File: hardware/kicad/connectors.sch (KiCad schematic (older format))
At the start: 1 part, among them J1 Conn_01x13_Male

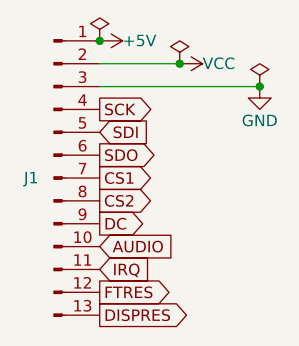
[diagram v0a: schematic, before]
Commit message: Clean up board and expose less debug signals
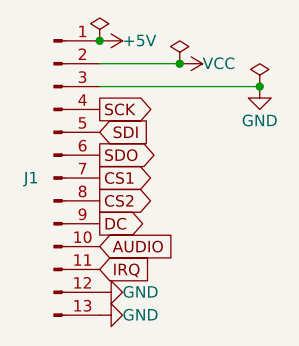
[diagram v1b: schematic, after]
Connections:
- net DISPRES is gone; now on net GND: J1.13 (Pin_13)
- net FTRES is gone; now on net GND: J1.12 (Pin_12)
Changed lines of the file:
@@
 Text GLabel 5650 4400 2    50   Input ~ 0
 IRQ
-Text GLabel 5650 4500 2    50   Output ~ 0
-FTRES
-Text GLabel 5650 4600 2    50   Output ~ 0
-DISPRES
+$Comp
+L power:GND #PWR029
+U 1 1 5F146BD0
+P 5650 4500
+F 0 "#PWR029" H 5650 4250 50  0001 C CNN
+F 1 "GND" V 5650 4400 50  0000 R CNN
+F 2 "" H 5650 4500 50  0001 C CNN
+F 3 "" H 5650 4500 50  0001 C CNN
+	1    5650 4500
+	0    -1   -1   0
+$EndComp
+$Comp
+L power:GND #PWR030
+U 1 1 5F146D3C
+P 5650 4600
+F 0 "#PWR030" H 5650 4350 50  0001 C CNN
+F 1 "GND" V 5650 4500 50  0000 R CNN
+F 2 "" H 5650 4600 50  0001 C CNN
+F 3 "" H 5650 4600 50  0001 C CNN
+	1    5650 4600
+	0    -1   -1   0
+$EndComp
 $EndSCHEMATC
